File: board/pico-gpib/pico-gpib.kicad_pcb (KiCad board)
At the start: 2 copper layers, 65 x 45 mm, 73 parts, among them J1 GPIB, J2 USB_B_Micro, J3 RasPi_Header_40W, J4 Debug, U1 RP2040, U2 SN75160BDW, U3 SN75162BDW, U4 W25Q128JVS, U5 NCP1117-3.3, U6 CAT24C32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

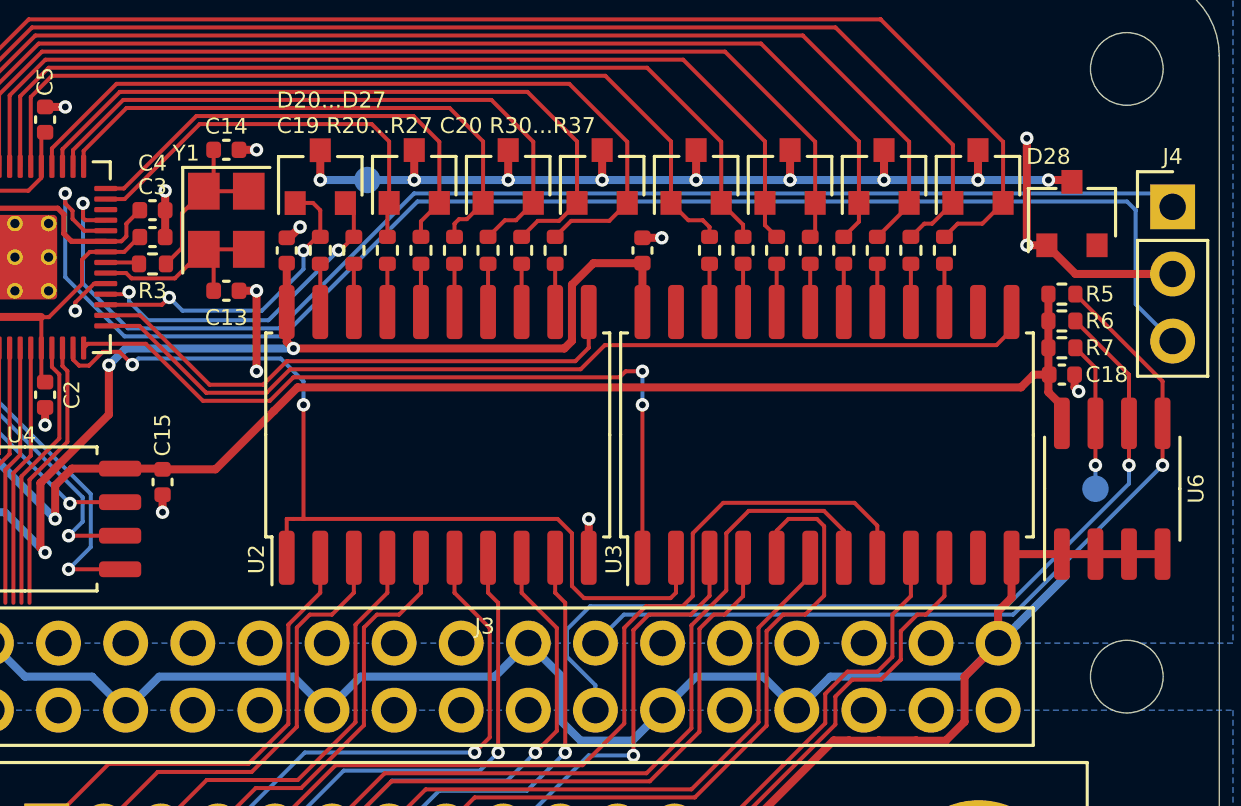
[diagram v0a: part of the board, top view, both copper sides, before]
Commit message: Move ID EEPROM to RPI 3V3 supply.
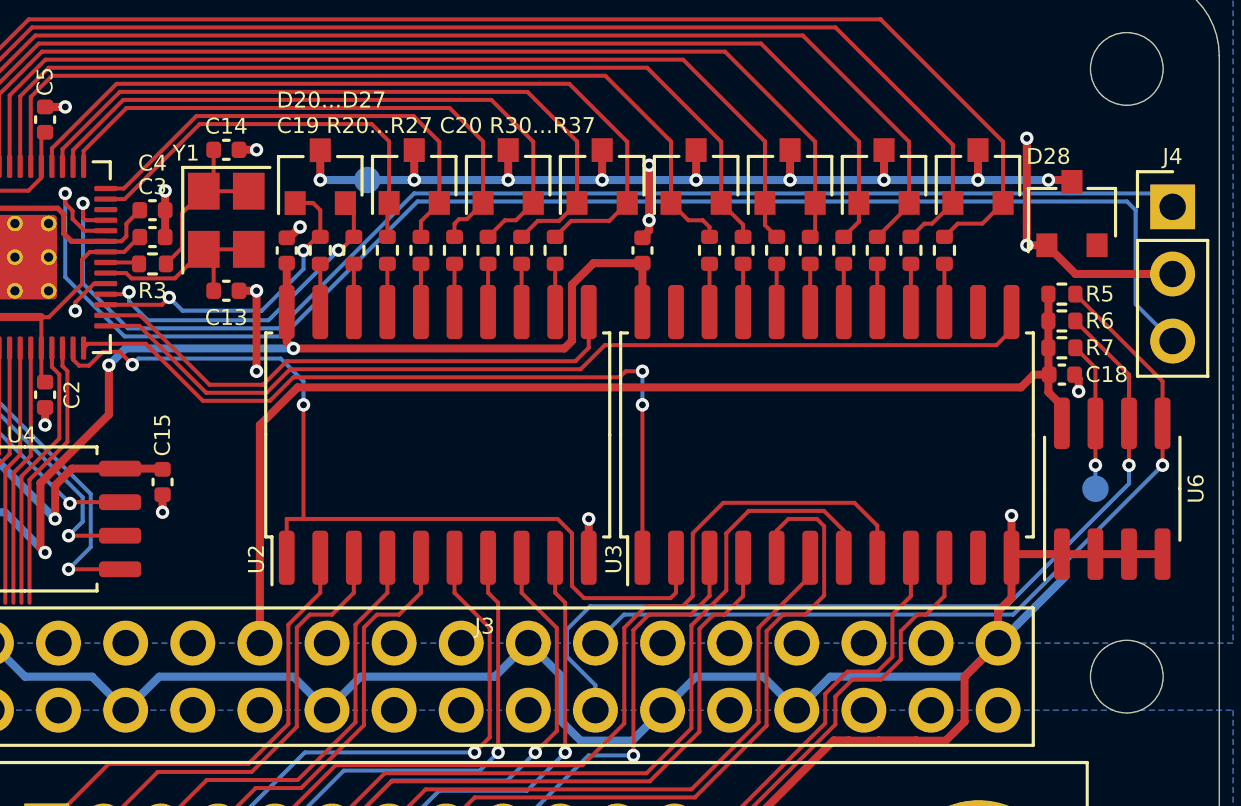
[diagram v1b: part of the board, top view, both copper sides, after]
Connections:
- net +5VP renamed +5V_PI
- C18 pad 1: +3V3 -> +3V3_PI
- J3 pad 17: Net-(J3-Pad17) -> +3V3_PI
- R5 pad 2: +3V3 -> +3V3_PI
- R6 pad 2: +3V3 -> +3V3_PI
- R7 pad 2: +3V3 -> +3V3_PI
- U6 pad 8: +3V3 -> +3V3_PI
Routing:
- net +3V3_PI: track 0.00 -> 44.7 mm
- net +3V3: track 103.8 -> 62.9 mm
- net GND: track 136.5 -> 140.2 mm, vias 21 -> 23
